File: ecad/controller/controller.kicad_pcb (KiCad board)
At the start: 2 copper layers, 43 x 68.3 mm, 15 parts, among them P1 USB_C_Plug_USB2.0, SW1 RST, SW2 BOOT, SW3 USER1, SW4 USER2, U1 ESP32-S3-WROOM-1, U2 AMS1117-3.3, U3 SN74LVC1T45DBV

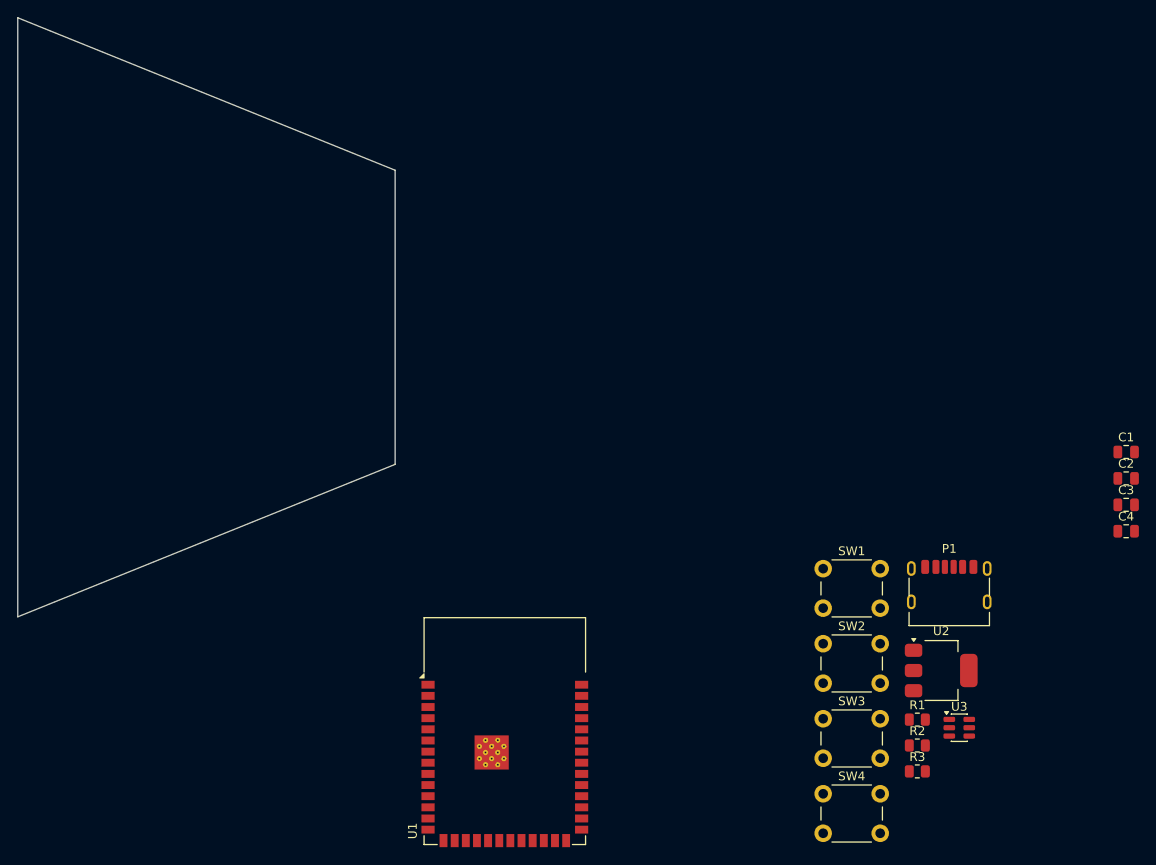
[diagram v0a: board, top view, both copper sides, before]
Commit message: split into 2 boards; switch led panel from 4 layers to 2 layers;
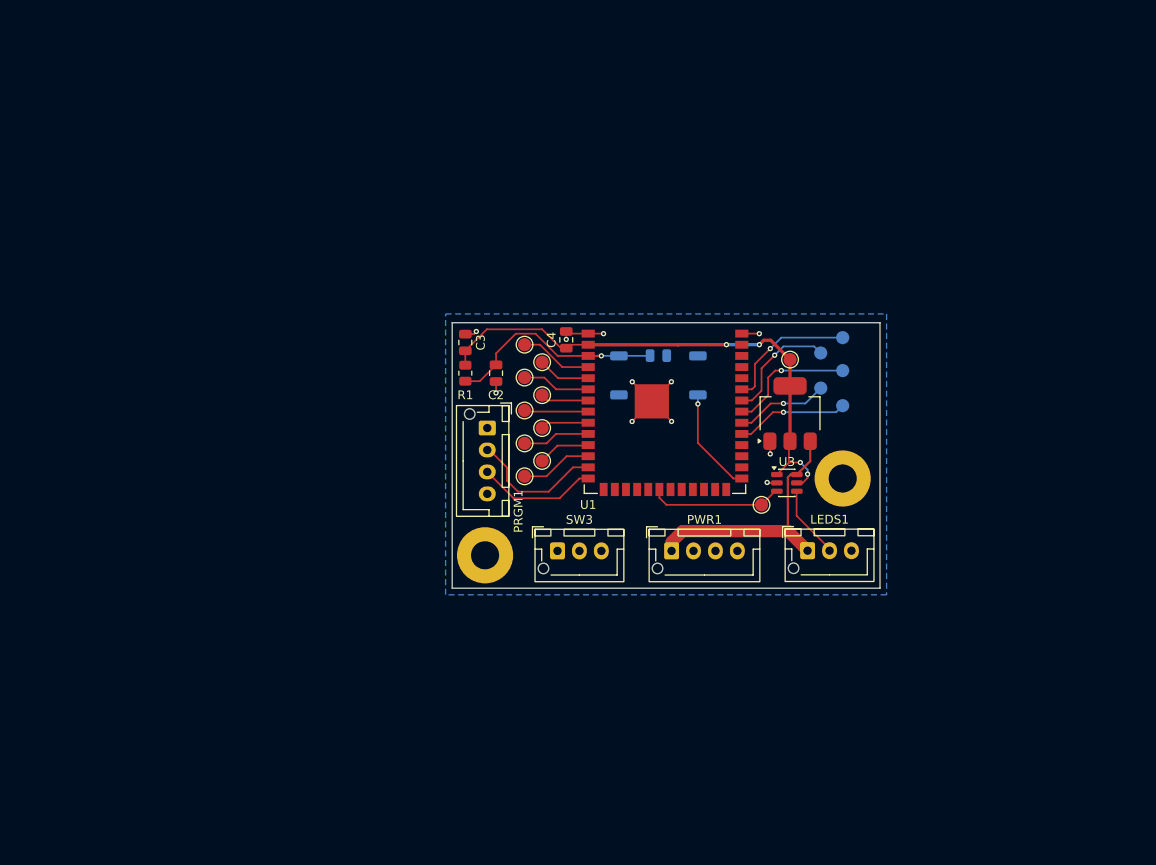
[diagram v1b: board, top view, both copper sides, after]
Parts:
- removed C1: 1uF, Capacitor_SMD:C_0805_2012Metric
- removed P1: USB_C_Plug_USB2.0, Connector_USB:USB_C_Receptacle_HRO_TYPE-C-31-M-17
- removed R2, R3: 5.1k, Resistor_SMD:R_0805_2012Metric
- removed SW4: USER2, Button_Switch_THT:SW_PUSH_6mm
- added 3V3: TestPoint, TestPoint:TestPoint_Pad_D1.5mm, F.Cu at (88.0, 39.0)
- added C5: 0.1uF, Capacitor_SMD:C_0805_2012Metric, B.Cu at (73.0, 38.5)
- added H1: MountingHole, MountingHole:MountingHole_3.2mm_M3_Pad, F.Cu at (94.0, 52.5)
- added H2: MountingHole, MountingHole:MountingHole_3.2mm_M3_Pad, F.Cu at (53.2, 61.2)
- added IO15: TestPoint, TestPoint:TestPoint_Pad_D1.5mm, F.Cu at (57.8, 44.8)
- added IO16: TestPoint, TestPoint:TestPoint_Pad_D1.5mm, F.Cu at (59.8, 46.8)
- added IO17: TestPoint, TestPoint:TestPoint_Pad_D1.5mm, F.Cu at (57.8, 48.5)
- added IO18: TestPoint, TestPoint:TestPoint_Pad_D1.5mm, F.Cu at (59.8, 50.5)
- added IO38: TestPoint, TestPoint:TestPoint_Pad_D1.5mm, B.Cu at (94.0, 44.2)
- added IO39: TestPoint, TestPoint:TestPoint_Pad_D1.5mm, B.Cu at (91.5, 42.2)
- added IO4: TestPoint, TestPoint:TestPoint_Pad_D1.5mm, F.Cu at (57.8, 37.2)
- added IO40: TestPoint, TestPoint:TestPoint_Pad_D1.5mm, B.Cu at (94.0, 40.2)
- added IO41: TestPoint, TestPoint:TestPoint_Pad_D1.5mm, B.Cu at (91.5, 38.2)
- added IO42: TestPoint, TestPoint:TestPoint_Pad_D1.5mm, B.Cu at (94.0, 36.5)
- added IO5: TestPoint, TestPoint:TestPoint_Pad_D1.5mm, F.Cu at (59.8, 39.2)
- added IO6: TestPoint, TestPoint:TestPoint_Pad_D1.5mm, F.Cu at (57.8, 41.0)
- added IO7: TestPoint, TestPoint:TestPoint_Pad_D1.5mm, F.Cu at (59.8, 43.0)
- added IO8: TestPoint, TestPoint:TestPoint_Pad_D1.5mm, F.Cu at (57.8, 52.2)
- added LEDS1: Conn_01x03, Connector_JST:JST_XH_B3B-XH-AM_1x03_P2.50mm_Vertical, F.Cu at (90.0, 60.7)
- added LED_TP1: TestPoint, TestPoint:TestPoint_Pad_D1.5mm, F.Cu at (84.8, 55.5)
- added PRGM1: Conn_01x04, Connector_JST:JST_XH_B4B-XH-AM_1x04_P2.50mm_Vertical, F.Cu at (53.5, 46.8)
- added PWR1: Conn_01x04, Connector_JST:JST_XH_B4B-XH-AM_1x04_P2.50mm_Vertical, F.Cu at (74.5, 60.8)
- C2: value 0.1uF -> 1uF
- SW1, SW2: footprint Button_Switch_THT:SW_PUSH_6mm -> Button_Switch_SMD:SW_SPST_TS-1088-xR020; moved to B.Cu
- SW3: footprint Button_Switch_THT:SW_PUSH_6mm -> Connector_JST:JST_XH_B3B-XH-AM_1x03_P2.50mm_Vertical
- moved C3 77.5 mm to (51.0, 37.0), turned to 90 degrees
- moved C2 72.8 mm to (54.5, 40.5), turned to -90 degrees
- moved C4 67.4 mm to (62.5, 36.7), turned to 90 degrees
- moved R1 64.9 mm to (51.0, 40.5), turned to -90 degrees
- moved U1 44.0 mm to (73.8, 41.2)
- moved SW3 35.8 mm to (61.5, 60.8)
- moved U3 34.1 mm to (87.6, 53.0)
- moved U2 34.0 mm to (88.0, 45.1), turned to 90 degrees
- moved SW2 33.7 mm to (77.5, 40.8), turned to -90 degrees
- moved SW1 32.0 mm to (68.5, 40.8), turned to 90 degrees
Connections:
- U1 pad 10: unconnected-(U1-IO17-Pad10) -> Net-(U1-IO17)
- U1 pad 11: unconnected-(U1-IO18-Pad11) -> Net-(U1-IO18)
- U1 pad 12: unconnected-(U1-IO8-Pad12) -> Net-(U1-IO8)
- U1 pad 31: unconnected-(U1-IO38-Pad31) -> Net-(U1-IO38)
- U1 pad 32: unconnected-(U1-IO39-Pad32) -> Net-(U1-IO39)
- U1 pad 33: unconnected-(U1-IO40-Pad33) -> Net-(U1-IO40)
- U1 pad 34: unconnected-(U1-IO41-Pad34) -> Net-(U1-IO41)
- U1 pad 35: unconnected-(U1-IO42-Pad35) -> Net-(U1-IO42)
- U1 pad 4: unconnected-(U1-IO4-Pad4) -> Net-(U1-IO4)
- U1 pad 5: unconnected-(U1-IO5-Pad5) -> Net-(U1-IO5)
- U1 pad 6: unconnected-(U1-IO6-Pad6) -> Net-(U1-IO6)
- U1 pad 7: unconnected-(U1-IO7-Pad7) -> Net-(U1-IO7)
- U1 pad 8: unconnected-(U1-IO15-Pad8) -> Net-(U1-IO15)
- U1 pad 9: unconnected-(U1-IO16-Pad9) -> Net-(U1-IO16)
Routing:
- net +3V3: track 0.00 -> 60.9 mm, vias 0 -> 4
- net +5V: track 0.00 -> 30.3 mm
- net GND: track 0.00 -> 25.2 mm, vias 0 -> 11
- net /EN: track 0.00 -> 25.2 mm, vias 0 -> 1
- net /D-: track 0.00 -> 15.5 mm
- net Net-(U1-IO42): track 0.00 -> 15.4 mm, vias 0 -> 1
- net /LED_GPIO: track 0.00 -> 15.3 mm
- net Net-(U1-IO40): track 0.00 -> 14.6 mm, vias 0 -> 1
- net /D+: track 0.00 -> 13.7 mm
- net Net-(U1-IO41): track 0.00 -> 13.4 mm, vias 0 -> 1
- net Net-(U1-IO38): track 0.00 -> 12.8 mm, vias 0 -> 1
- net /IO0: track 0.00 -> 12.2 mm, vias 0 -> 1
- net Net-(U1-IO39): track 0.00 -> 10.6 mm, vias 0 -> 1
- net Net-(U1-IO4): track 0.00 -> 8.81 mm
- net Net-(U1-IO6): track 0.00 -> 8.31 mm
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- added copper zone on B.Cu, net GND
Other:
- board size 43 x 68.3 mm -> 48.8 x 30.2 mm

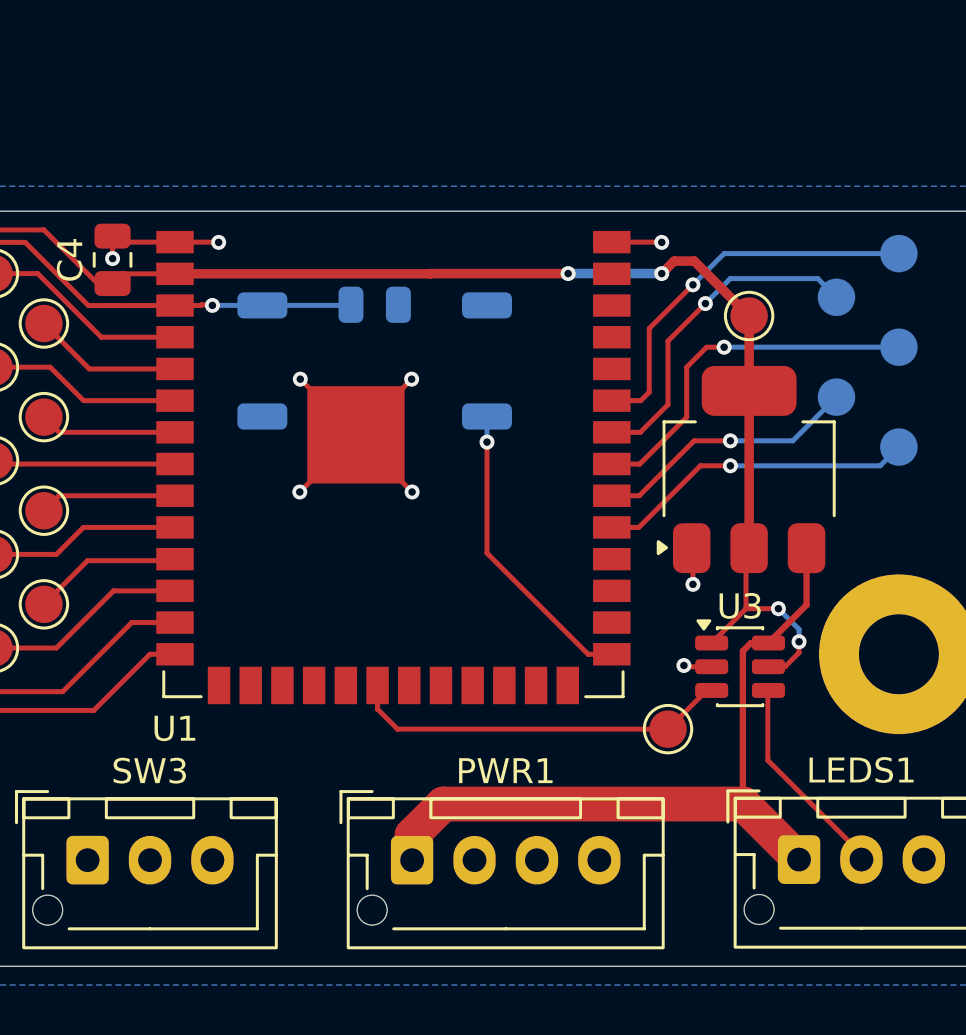
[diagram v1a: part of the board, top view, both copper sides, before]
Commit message: added vertical USB-C connector to controller board; and possibly much more
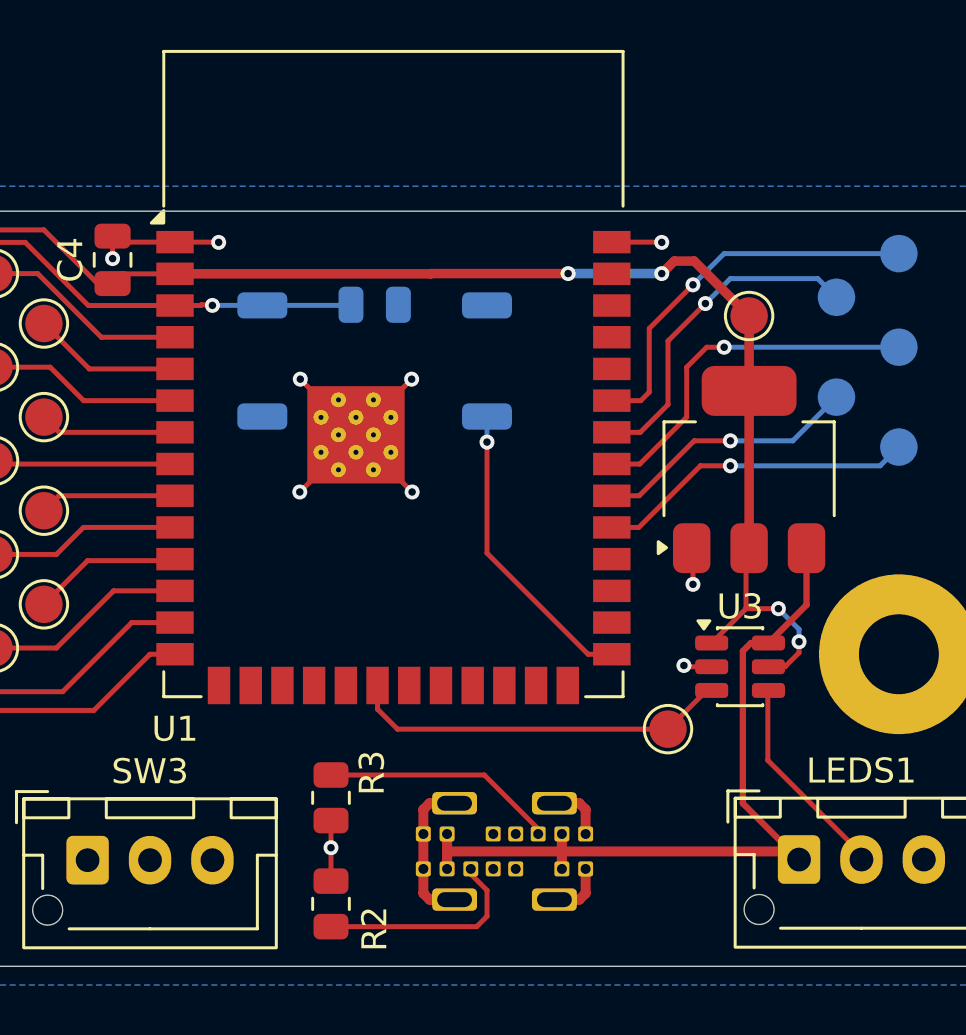
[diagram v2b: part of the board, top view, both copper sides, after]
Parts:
- removed PWR1: Conn_01x04, Connector_JST:JST_XH_B4B-XH-AM_1x04_P2.50mm_Vertical
- added J1: USB_C_Receptacle, usb-library:USB-C-VERTICAL-14P, B.Cu at (78.2, 60.4)
- added R2: 10kΩ, Resistor_SMD:R_0805_2012Metric, F.Cu at (71.2, 62.5)
- added R3: 10kΩ, Resistor_SMD:R_0805_2012Metric, F.Cu at (71.2, 58.2)
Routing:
- net GND: track 25.2 -> 38.7 mm, vias 11 -> 12
- net Net-(J1-CC1): track 0.00 -> 9.40 mm
- net Net-(J1-CC2): track 0.00 -> 8.59 mm
- net +5V: track 30.3 -> 35.4 mm

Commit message: who knows
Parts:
- SW3: footprint Connector_JST:JST_XH_B3B-XH-AM_1x03_P2.50mm_Vertical -> Button_Switch_SMD:SW_Push_1P1T_NO_E-Switch_TL3301NxxxxxG; moved to B.Cu
- moved SW3 18.7 mm to (78.2, 52.5)

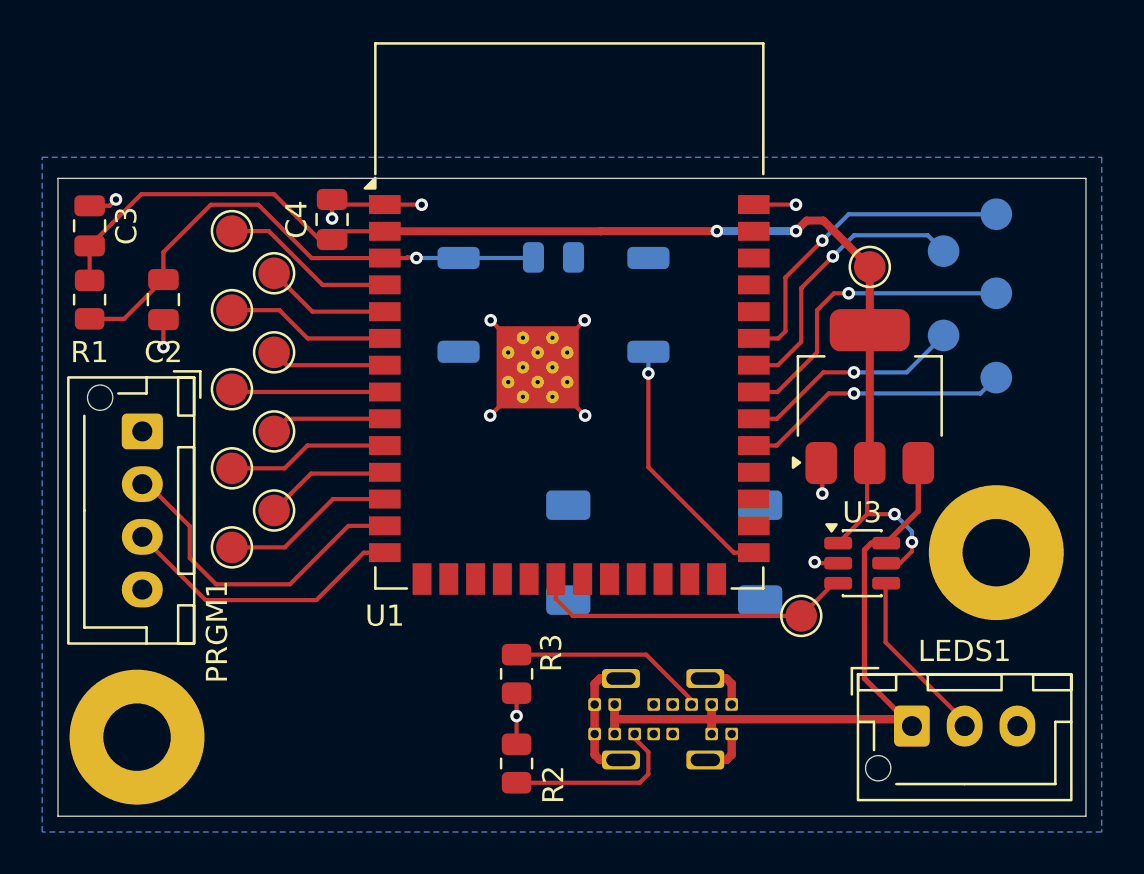
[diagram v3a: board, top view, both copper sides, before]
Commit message: add ESD protection; change USB connectors; ajust ESP32 pinout; more
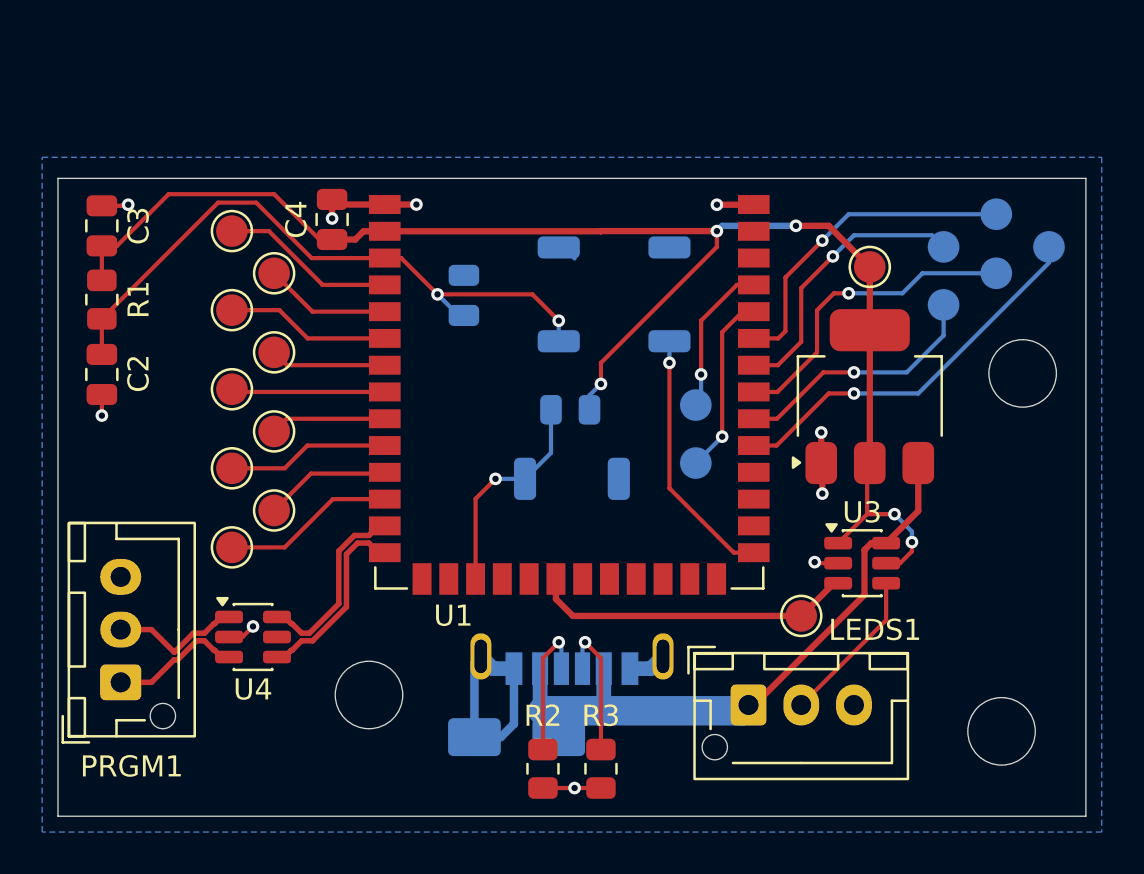
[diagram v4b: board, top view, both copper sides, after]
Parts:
- removed J1: USB_C_Receptacle, usb-library:USB-C-VERTICAL-14P
- added D1: SMAJ5.0CA, Diode_SMD:D_SMA, B.Cu at (71.2, 61.2)
- added H3: MountingHole, MountingHole:MountingHole_3.2mm_M3, F.Cu at (94.2, 61.0)
- added J2: USB_C_Receptacle_PowerOnly_6P, usb-c:usb-c-vertical-smd, B.Cu at (73.9, 58.0)
- added R4: 10kΩ, Resistor_SMD:R_0805_2012Metric, B.Cu at (73.8, 45.7)
- added RXD0: TestPoint, TestPoint:TestPoint_Pad_D1.5mm, B.Cu at (79.8, 48.2)
- added TXD0: TestPoint, TestPoint:TestPoint_Pad_D1.5mm, B.Cu at (79.8, 45.5)
- added U4: USBLC6-2SC6, Package_TO_SOT_SMD:SOT-23-6, F.Cu at (58.8, 56.5)
- H1, H2: footprint MountingHole:MountingHole_3.2mm_M3_Pad -> MountingHole:MountingHole_3.2mm_M3
- PRGM1: value Conn_01x04 -> Conn_01x03; footprint Connector_JST:JST_XH_B4B-XH-AM_1x04_P2.50mm_Vertical -> Connector_JST:JST_XH_B3B-XH-AM_1x03_P2.50mm_Vertical
- R2, R3: value 10kΩ -> 5.1kΩ
- SW3: footprint Button_Switch_SMD:SW_Push_1P1T_NO_E-Switch_TL3301NxxxxxG -> Button_Switch_SMD:SW_SPST_TS-1088-xR020
- moved PRGM1 11.9 mm to (52.5, 58.6), turned to 90 degrees
- moved H2 11.2 mm to (64.2, 59.2)
- moved H1 8.59 mm to (95.2, 44.0)
- moved LEDS1 7.81 mm to (82.2, 59.7)
- moved IO38 6.69 mm to (96.5, 38.0)
- moved R3 6.02 mm to (75.2, 62.8)
- moved SW3 5.60 mm to (73.9, 49.0), turned to 180 degrees
- moved SW1 4.78 mm to (73.2, 40.2), turned to -90 degrees
- moved C5 4.62 mm to (68.8, 40.3), turned to 90 degrees
- moved C2 4.60 mm to (51.6, 44.0)
- moved IO39 1.45 mm to (91.5, 40.8)
- moved R2 1.27 mm to (72.5, 62.8), turned to -90 degrees
- moved SW2 1.12 mm to (78.5, 40.2)
- moved IO40 0.95 mm to (94.0, 39.2)
- moved C3 0.58 mm to (51.6, 37.0)
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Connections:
- PRGM1 pad 1: unconnected-(PRGM1-Pin_1-Pad1) -> /IN_D+
- PRGM1 pad 2: /D- -> /IN_D-
- PRGM1 pad 3: /D+ -> GND
- SW3 pad 2: unconnected-(SW3-Pad2) -> /SWITCH
- U1 pad 13: /D- -> /USB_D-
- U1 pad 14: /D+ -> /USB_D+
- U1 pad 17: unconnected-(U1-IO9-Pad17) -> /SWITCH
- U1 pad 36: unconnected-(U1-RXD0-Pad36) -> Net-(U1-RXD0)
- U1 pad 37: unconnected-(U1-TXD0-Pad37) -> Net-(U1-TXD0)
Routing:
- net /D-: track 15.5 -> 0.00 mm
- net /D+: track 13.7 -> 0.00 mm
- net /SWITCH: track 0.00 -> 10.3 mm, vias 0 -> 1
- net +3V3: track 60.9 -> 71.0 mm, vias 4 -> 5
- net GND: track 38.7 -> 29.5 mm, vias 12 -> 10
- net /USB_D+: track 0.00 -> 9.00 mm
- net /USB_D-: track 0.00 -> 9.00 mm
- net Net-(U1-RXD0): track 0.00 -> 8.63 mm, vias 0 -> 1
- net Net-(U1-TXD0): track 0.00 -> 7.31 mm, vias 0 -> 1
- net /IN_D-: track 0.00 -> 6.27 mm
- net /IN_D+: track 0.00 -> 6.27 mm
- net /EN: track 25.2 -> 30.9 mm, vias 1 -> 2
- net Net-(U1-IO38): track 12.8 -> 18.3 mm
- net +5V: track 35.4 -> 30.0 mm
- net Net-(J2-CC1): track 9.40 -> 6.70 mm, vias 0 -> 1
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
